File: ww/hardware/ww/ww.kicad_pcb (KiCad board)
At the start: 2 copper layers, 31 x 38 mm, 49 parts, among them J1 USB_B, J2 Conn_ARM_JTAG_SWD_10, SW1 BTN0, SW2 BTN1, U1 MCP73812T-420I-OT, U10 APA102, U11 APA102, U12 APA102, U13 APA102, U14 APA102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

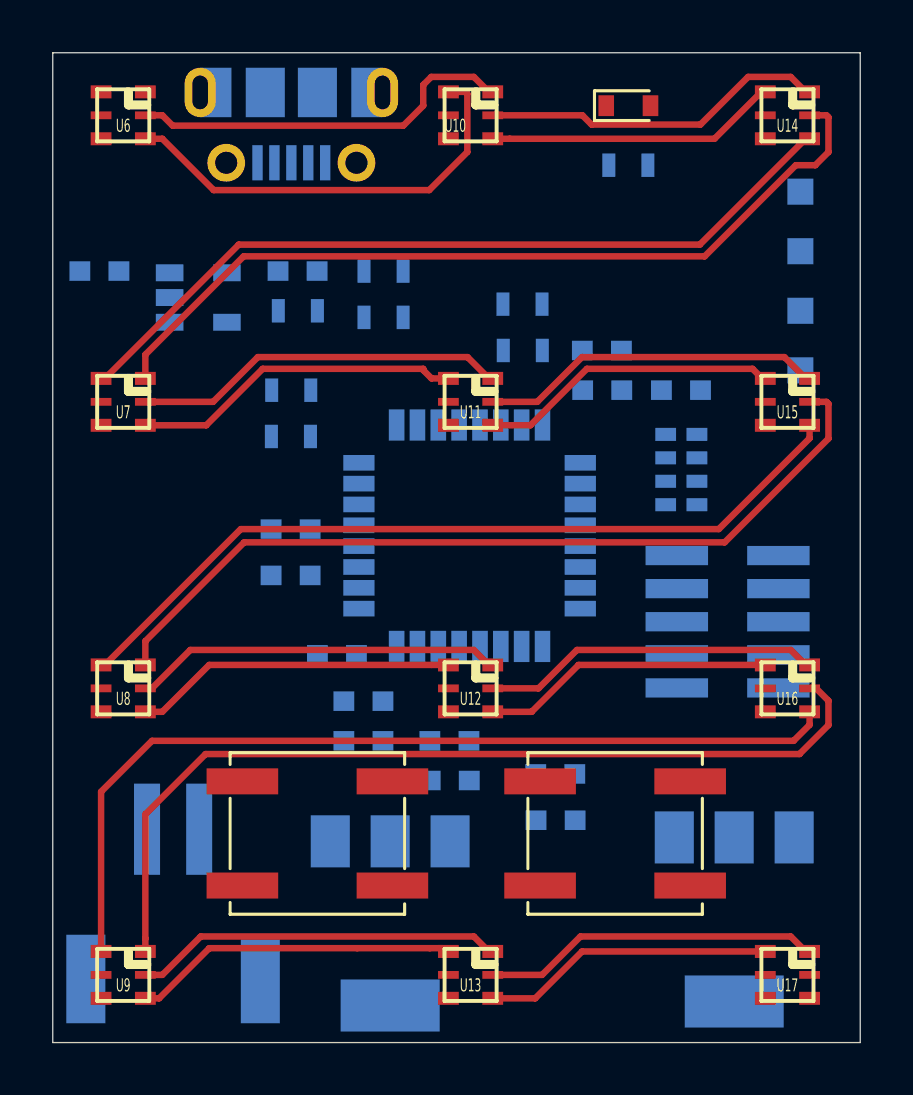
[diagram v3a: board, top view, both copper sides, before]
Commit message: Rip out all the emmc stuff, just a samd with lights
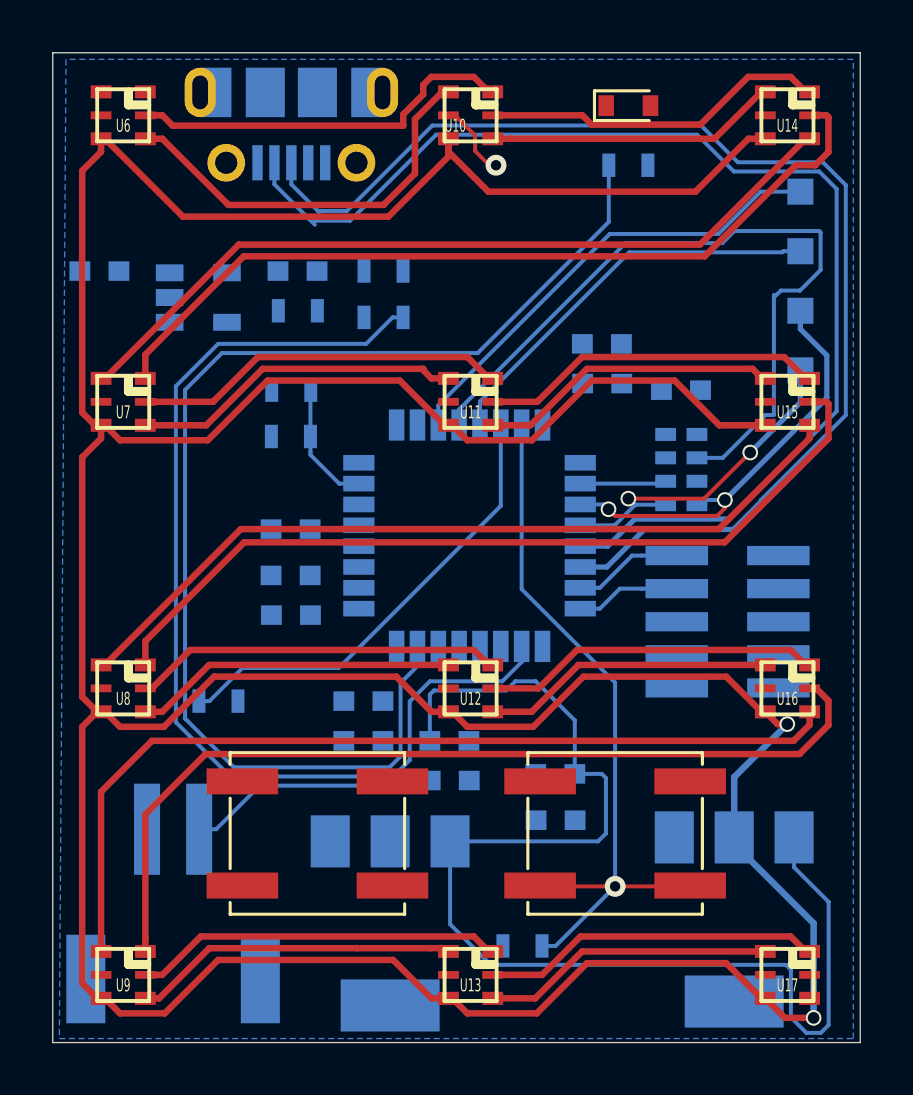
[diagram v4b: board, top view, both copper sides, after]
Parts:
- moved R8 24.6 mm to (56.1, 58.9), turned to 0 degrees
- moved R6 17.8 mm to (44.5, 49.5)
- moved C5 2.33 mm to (47.2, 46.2)
- moved C4 0.25 mm to (59.2, 37.3)
- moved C8 0.25 mm to (59.2, 35.8)
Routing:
- net +5V: track 0.00 -> 168.8 mm, vias 0 -> 2
- net Net-(BT1-Pad1): track 0.00 -> 56.5 mm
- net Net-(R7-Pad1): track 0.00 -> 47.4 mm
- net /USB_DP: track 0.00 -> 46.6 mm
- net /USB_DM: track 0.00 -> 46.0 mm
- net /CEN: track 0.00 -> 40.7 mm
- net /RTC_IRQ: track 0.00 -> 29.3 mm
- net Net-(R8-Pad2): track 0.00 -> 28.7 mm, vias 0 -> 1
- net /LED_CLK: track 0.00 -> 18.1 mm
- net Net-(R6-Pad2): track 0.00 -> 17.8 mm
- net /RTC_SCL: track 0.00 -> 16.6 mm, vias 0 -> 2
- net /LED_SDI: track 0.00 -> 15.6 mm
- net /RTC_SDA: track 0.00 -> 13.3 mm, vias 0 -> 2
- net /VLEV: track 0.00 -> 4.80 mm
- net /SWDIO: track 0.00 -> 4.22 mm
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- added copper zone on B.Cu, net GND
